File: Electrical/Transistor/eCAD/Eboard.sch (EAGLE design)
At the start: 29 parts

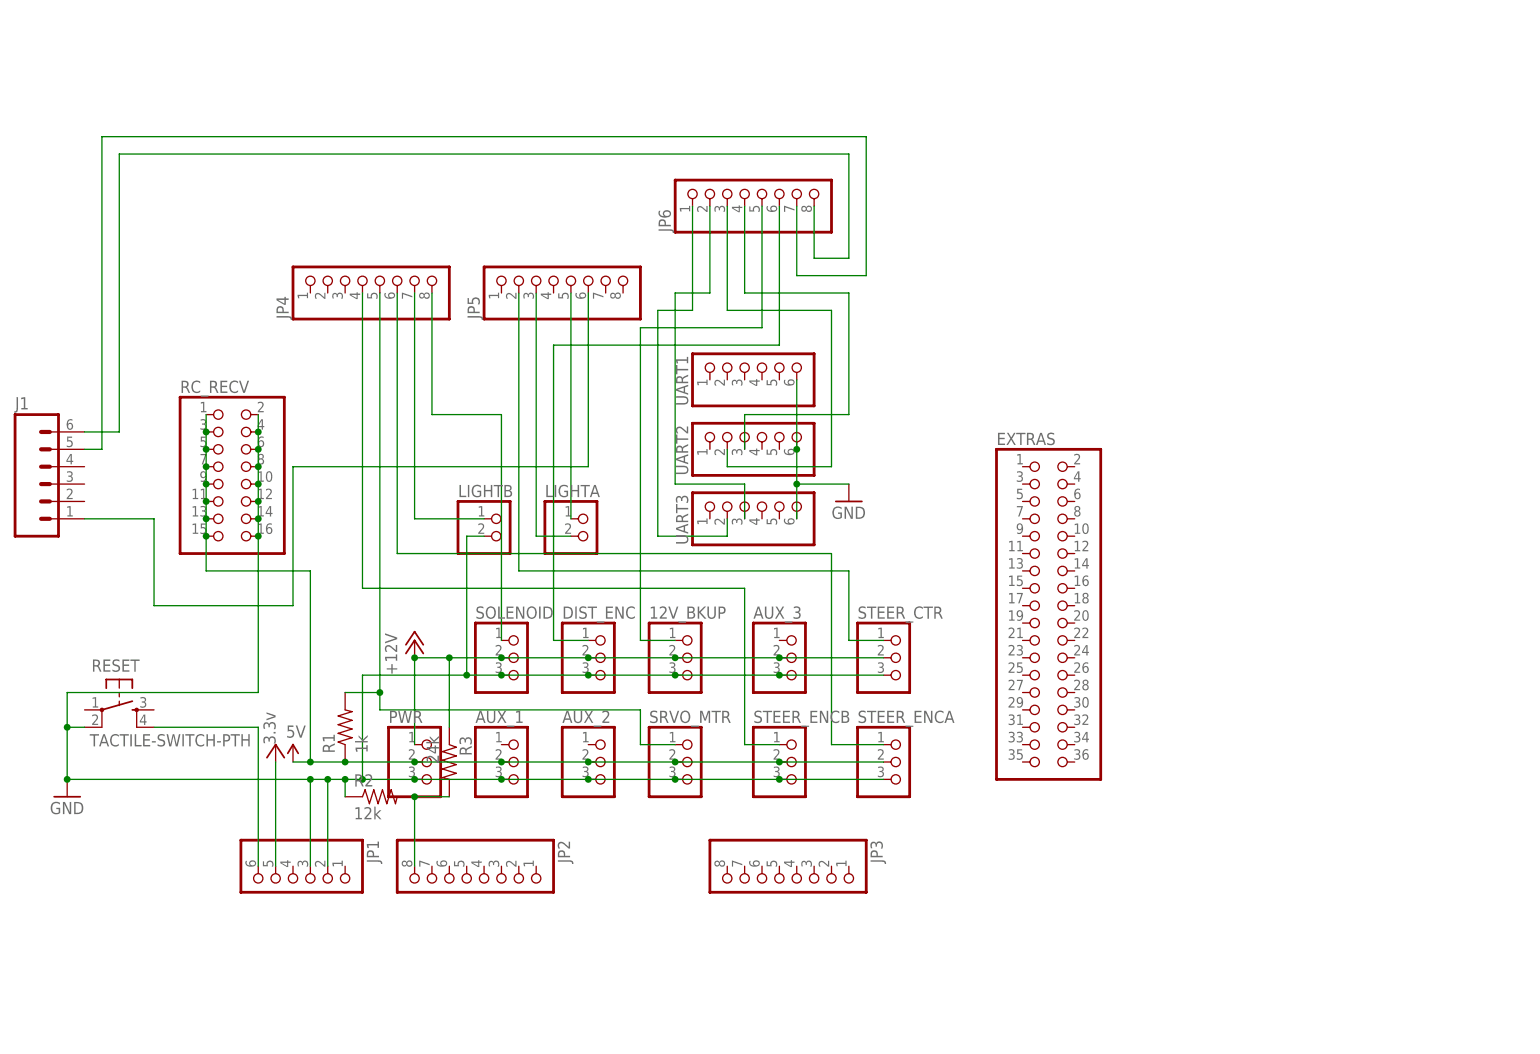
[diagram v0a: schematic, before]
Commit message: shield updated with indicator lights, deleted excess pins, condensed encoder pins, deleted two aux pins, thickened 12V and 5V lines, connected 2 UARTs, 2 2-pin LEDs became 1 4-pin
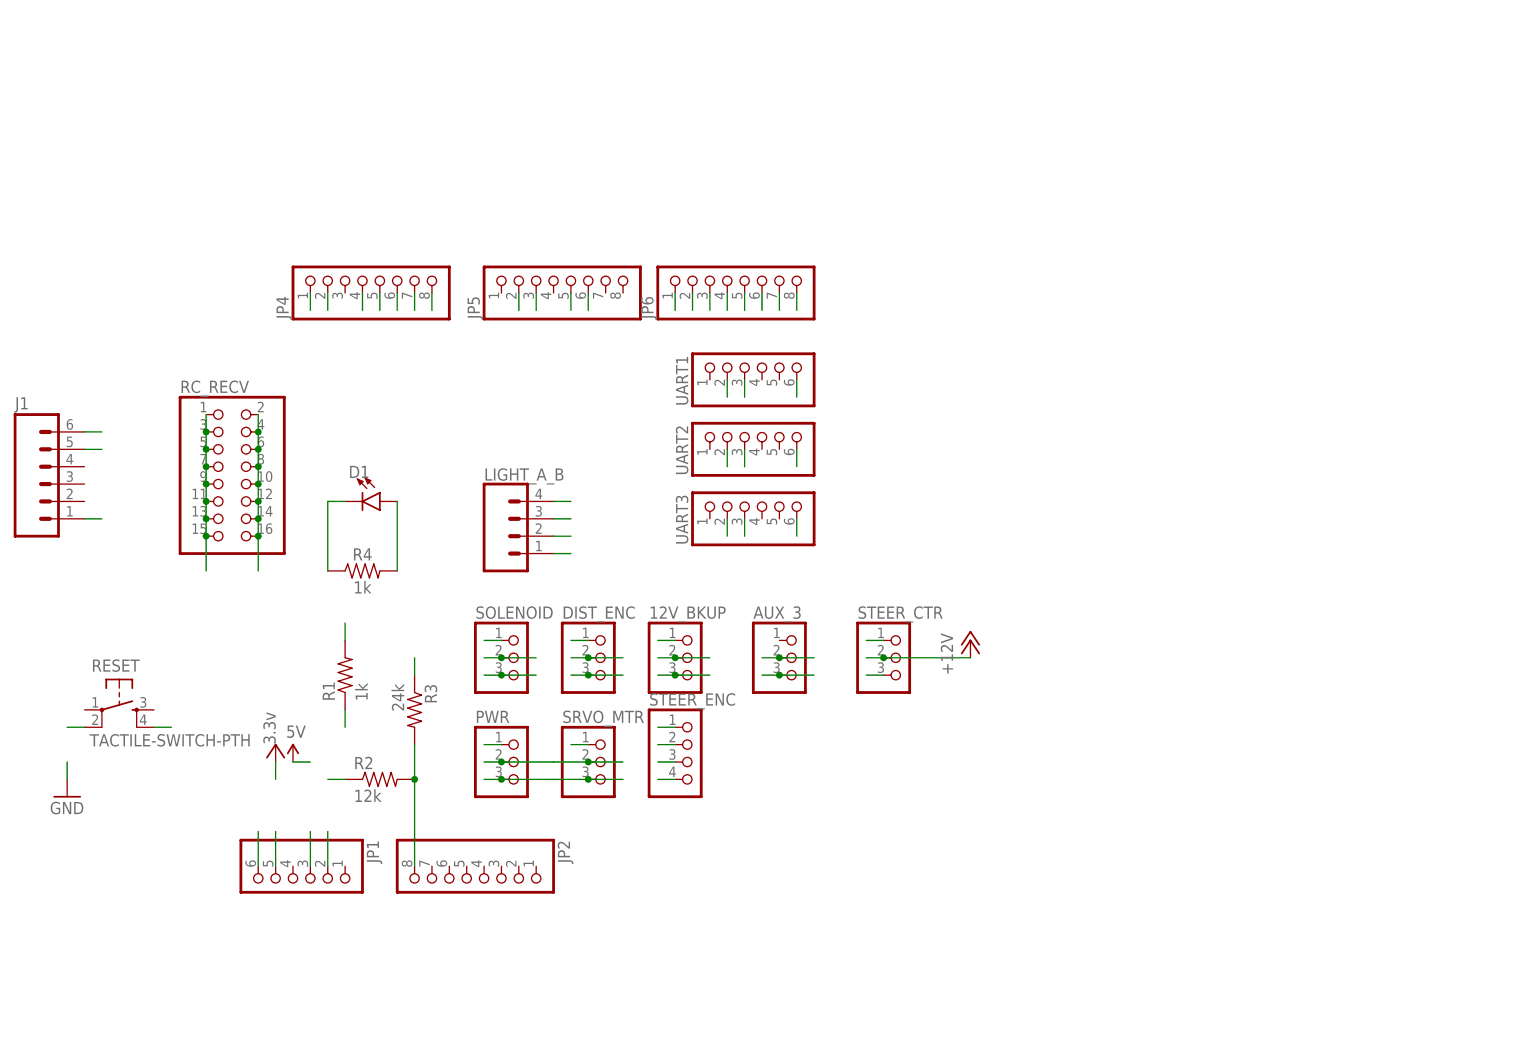
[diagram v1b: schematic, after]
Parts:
- removed AUX_1, AUX_2, STEER_ENCA, STEER_ENCB: (no value), pinhead:PINHD-1X3
- removed EXTRAS: (no value), pinhead:PINHD-2X18
- removed JP3: (no value), pinhead:PINHD-1X8
- removed LIGHTA, LIGHTB: (no value), pinhead:PINHD-1X2
- added D1: (no value), SparkFun-LED:LED1206
- added LIGHT_A_B: (no value), SparkFun-Connectors:CONN_04
- added R4: 1k, SparkFun-Resistors:1KOHM-HORIZ-1/4W-5%
- added STEER_ENC: (no value), pinhead:PINHD-1X4
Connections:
- net +12V renamed 12V
- net N$11 renamed UART3_TX
- net N$12 renamed UART3_RX
- net N$13 renamed UART2_TX
- net N$14 renamed UART2_RX
- net N$15 renamed J1_5
- net N$16 renamed J1_1
- net N$3 renamed J1_6
- net N$6 renamed SOLENOID
- net N$7 renamed STEER_CTR
- net N$8 renamed SRVO_MTR
- removed net N$1: JP2.8, R2.2, R3.2
- removed net N$10: JP4.6, STEER_ENCA.1
- removed net N$17: JP5.5, LIGHTA.1
- removed net N$18: JP5.3, LIGHTA.2
- removed net N$2: JP4.7, LIGHTB.1
- removed net N$9: JP4.4, STEER_ENCB.1
- removed net RESET: JP1.6, RESET.4
- new net 12V_BKUP: 12V_BKUP.1, JP4.1
- new net DIST_ENC: DIST_ENC.1, JP4.2
- new net LIGHT_A1: JP5.5, LIGHT_A_B.4
- new net LIGHT_A2: JP5.3, LIGHT_A_B.3
- new net LIGHT_B: JP4.7, LIGHT_A_B.2
- new net STEER_ENC1: JP4.4, STEER_ENC.1
- new net STEER_ENC2: JP4.6, STEER_ENC.2
- new net UART1_RX: JP6.6, UART1.3
- new net UART1_TX: JP6.5, UART1.2
- net 5V: now also D1.A, R4.2, STEER_ENC.3; no longer AUX_1.2, AUX_2.2, STEER_ENCA.2, STEER_ENCB.2
- net GND: now also D1.C, JP2.8, LIGHT_A_B.1, R2.2, R3.2, R4.1, STEER_ENC.4; no longer AUX_1.3, AUX_2.3, LIGHTB.2, STEER_ENCA.3, STEER_ENCB.3
- net N$4: now also JP1.6; no longer DIST_ENC.1, JP6.6
- net N$5: now also RESET.4; no longer 12V_BKUP.1, JP6.5
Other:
- moved on the sheet: JP6, PWR, R1, R2, R3, SRVO_MTR

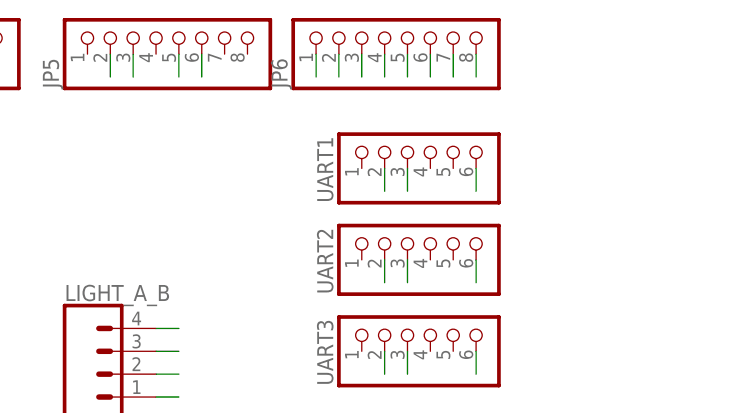
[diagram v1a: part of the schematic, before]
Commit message: deleted UART1 because conflicts with the servo
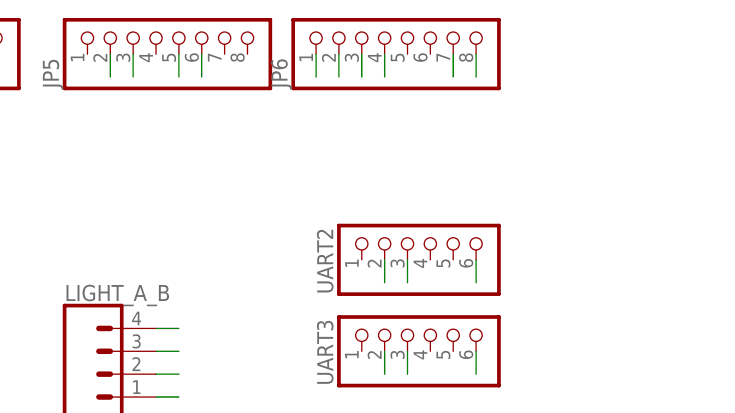
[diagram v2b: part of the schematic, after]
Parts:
- removed UART1: (no value), pinhead:PINHD-1X6
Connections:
- removed net UART1_RX: JP6.6, UART1.3
- removed net UART1_TX: JP6.5, UART1.2
- net GND: no longer UART1.6
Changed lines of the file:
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@@
 <part name="P+1" library="supply1" deviceset="VCC" device="" value="3.3v"/>
 <part name="SOLENOID" library="pinhead" deviceset="PINHD-1X3" device=""/>
-<part name="UART1" library="pinhead" deviceset="PINHD-1X6" device=""/>
 <part name="UART2" library="pinhead" deviceset="PINHD-1X6" device=""/>
 <part name="UART3" library="pinhead" deviceset="PINHD-1X6" device=""/>
@@
 </instance>
 <instance part="SOLENOID" gate="A" x="76.2" y="86.36"/>
-<instance part="UART1" gate="A" x="111.76" y="129.54" rot="R90"/>
 <instance part="UART2" gate="A" x="111.76" y="119.38" rot="R90"/>
 <instance part="UART3" gate="A" x="111.76" y="109.22" rot="R90"/>
@@
 </segment>
 <segment>
-<pinref part="UART1" gate="A" pin="6"/>
-<wire x1="116.84" y1="127" x2="116.84" y2="124.46" width="0.1524" layer="91"/>
-</segment>
-<segment>
 <pinref part="UART3" gate="A" pin="6"/>
 <wire x1="116.84" y1="106.68" x2="116.84" y2="104.14" width="0.1524" layer="91"/>
@@
 </segment>
 </net>
-<net name="UART1_TX" class="0">
-<segment>
-<pinref part="UART1" gate="A" pin="2"/>
-<wire x1="106.68" y1="127" x2="106.68" y2="124.46" width="0.1524" layer="91"/>
-</segment>
-<segment>
-<pinref part="JP6" gate="A" pin="5"/>
-<wire x1="109.22" y1="139.7" x2="109.22" y2="137.16" width="0.1524" layer="91"/>
-</segment>
-</net>
-<net name="UART1_RX" class="0">
-<segment>
-<pinref part="UART1" gate="A" pin="3"/>
-<wire x1="109.22" y1="127" x2="109.22" y2="124.46" width="0.1524" layer="91"/>
-</segment>
-<segment>
-<pinref part="JP6" gate="A" pin="6"/>
-<wire x1="111.76" y1="139.7" x2="111.76" y2="137.16" width="0.1524" layer="91"/>
-</segment>
-</net>

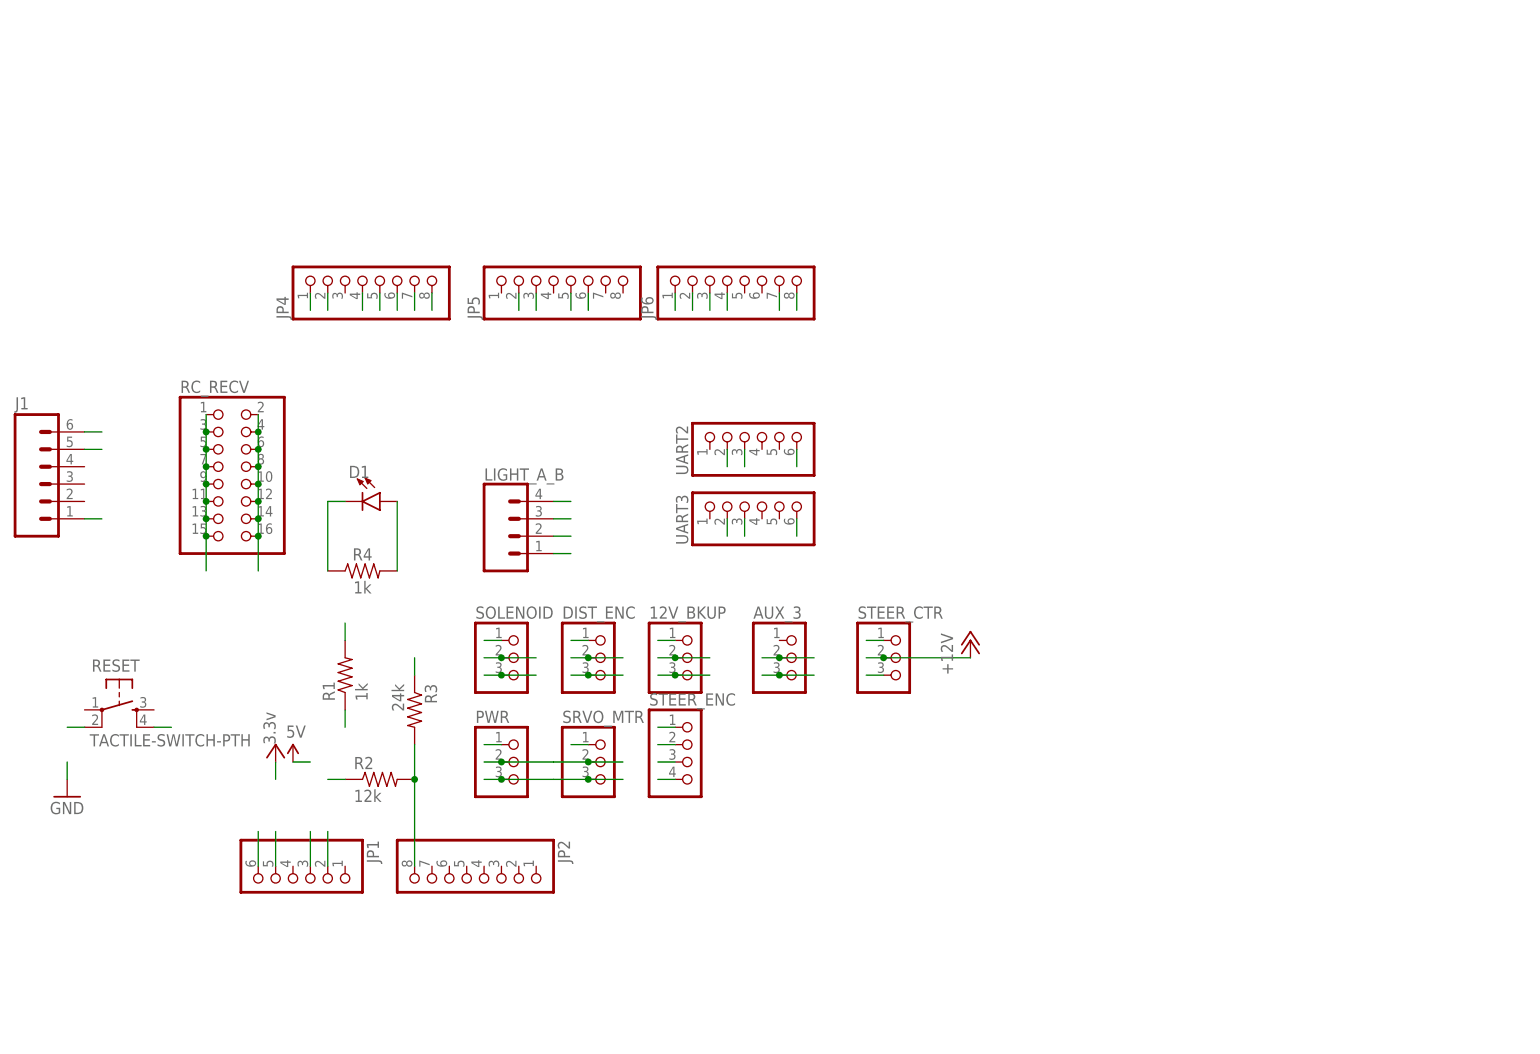
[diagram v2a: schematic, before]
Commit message: deleted 12V_BKUP and AUX_3, as well as labelled everything. did not update .brd file yet.
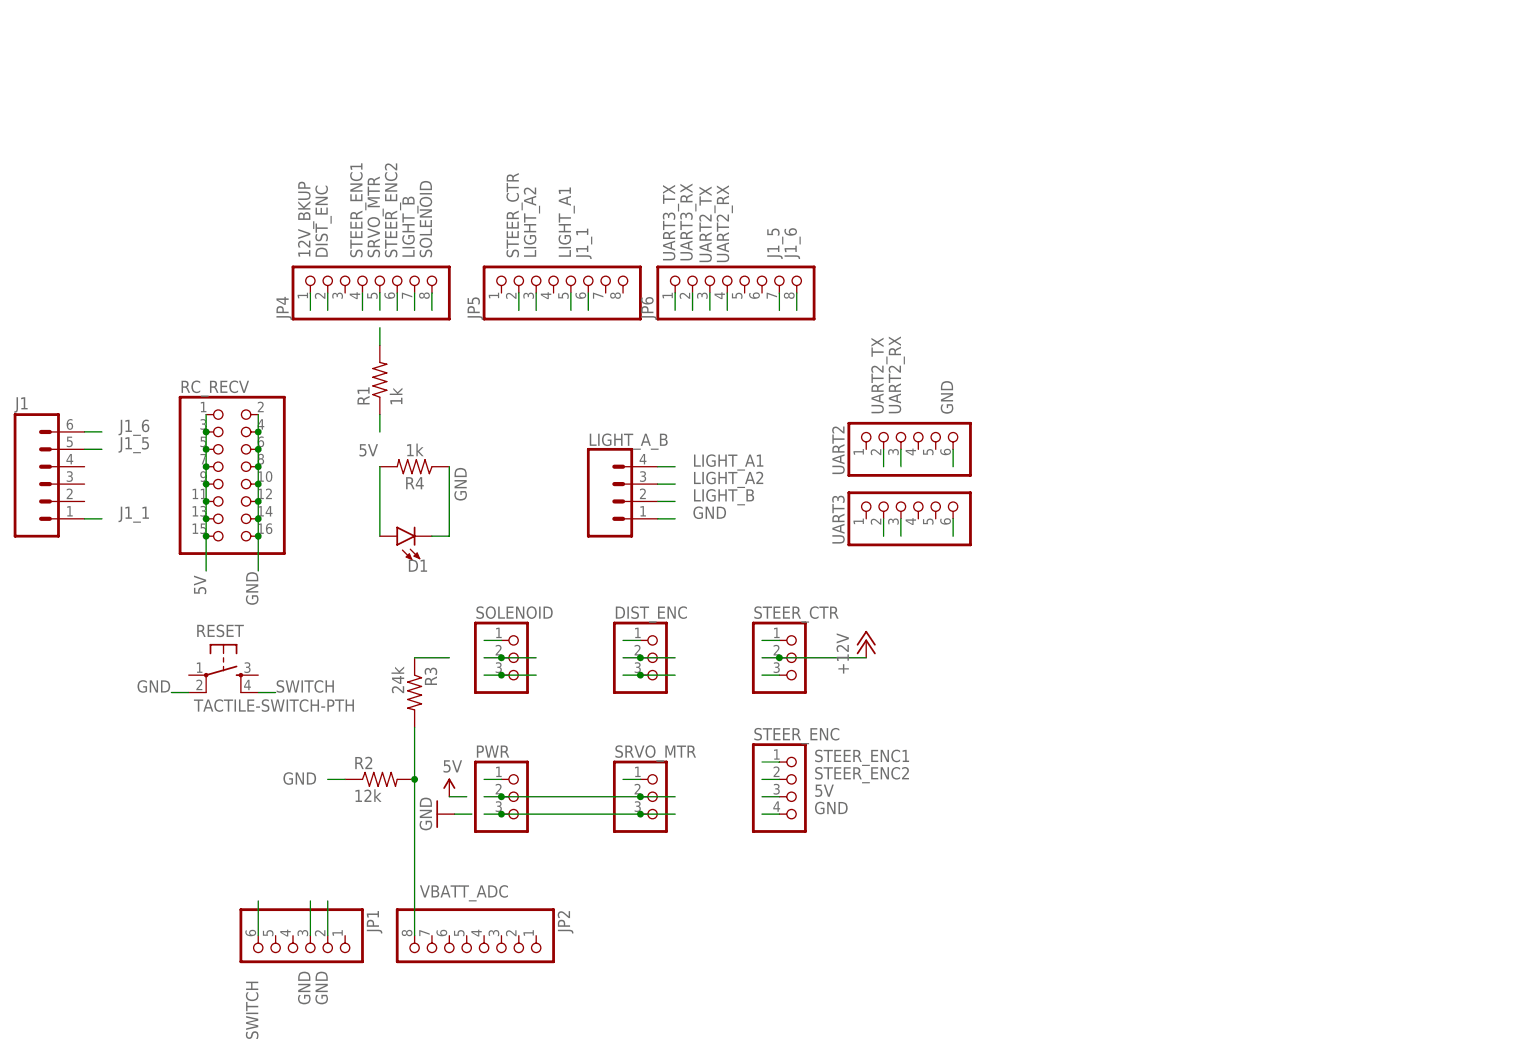
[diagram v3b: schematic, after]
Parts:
- removed 12V_BKUP, AUX_3: (no value), pinhead:PINHD-1X3
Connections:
- removed net N$4: JP1.6
- removed net N$5: RESET.4
- removed net VCC: JP1.5
- new net SWITCH: JP1.6, RESET.4
- new net VBATT_ADC: JP2.8, R2.2, R3.2
- net 12V: no longer 12V_BKUP.2, AUX_3.2
- net 12V_BKUP: no longer 12V_BKUP.1
- net GND: no longer 12V_BKUP.3, AUX_3.3, JP2.8, R2.2, R3.2
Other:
- moved on the sheet: D1, DIST_ENC, JP1, JP2, LIGHT_A_B, PWR, R1, R3, R4, RESET, SRVO_MTR, STEER_CTR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

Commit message: made all the lines on schematic uniform, added ground and 5V symbols, rearranged groupings for ease of understanding, rerouted board so that wires were less messy, added 5V diode silkscreen
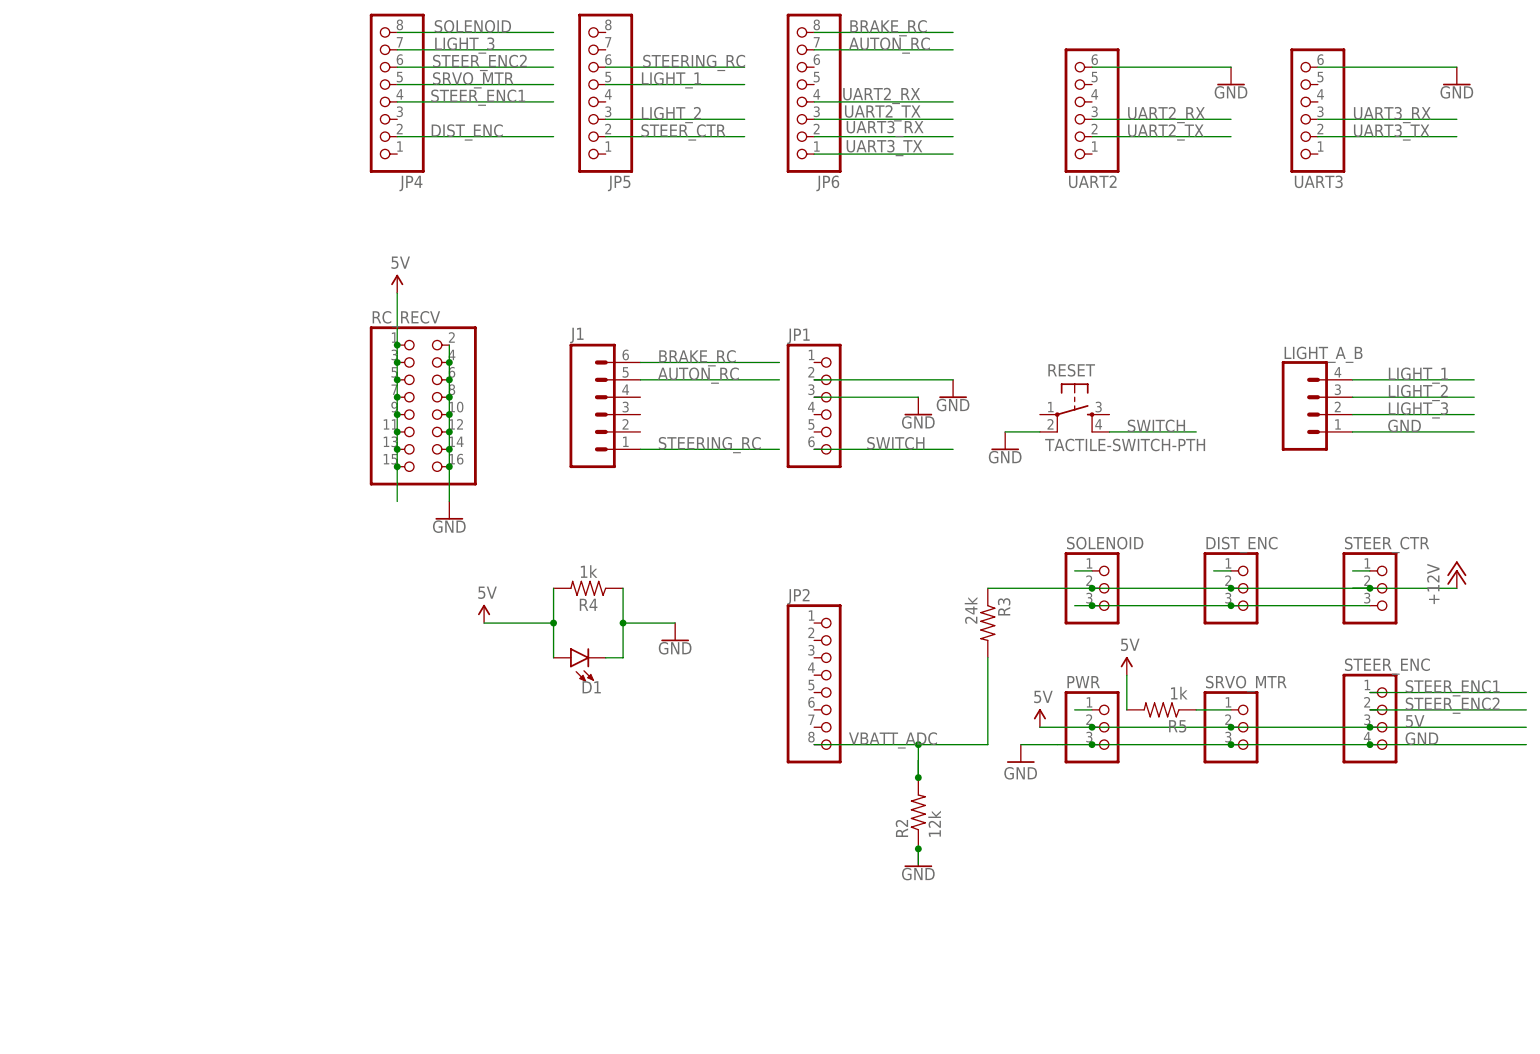
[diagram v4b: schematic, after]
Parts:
- removed R1: 1k, SparkFun-Resistors:1KOHM-1/4W-5%(PTH)
- added R5: 1k, SparkFun-Resistors:1KOHM-1/4W-5%(PTH)
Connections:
- net J1_1 renamed STEERING_RC
- net J1_5 renamed AUTON_RC
- net J1_6 renamed BRAKE_RC
- net LIGHT_A1 renamed LIGHT_1
- net LIGHT_A2 renamed LIGHT_2
- net LIGHT_B renamed LIGHT_3
- removed net 12V_BKUP: JP4.1
- net 5V: now also R5.2; no longer R1.1
- net SRVO_MTR: now also R5.1; no longer R1.2
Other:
- moved on the sheet: D1, DIST_ENC, J1, JP1, JP2, JP4, JP5, JP6, LIGHT_A_B, PWR, R2, R3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
